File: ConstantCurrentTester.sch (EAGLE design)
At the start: 3 parts, among them U1 ATMEGA328PQFN_32, Y1 8MHz

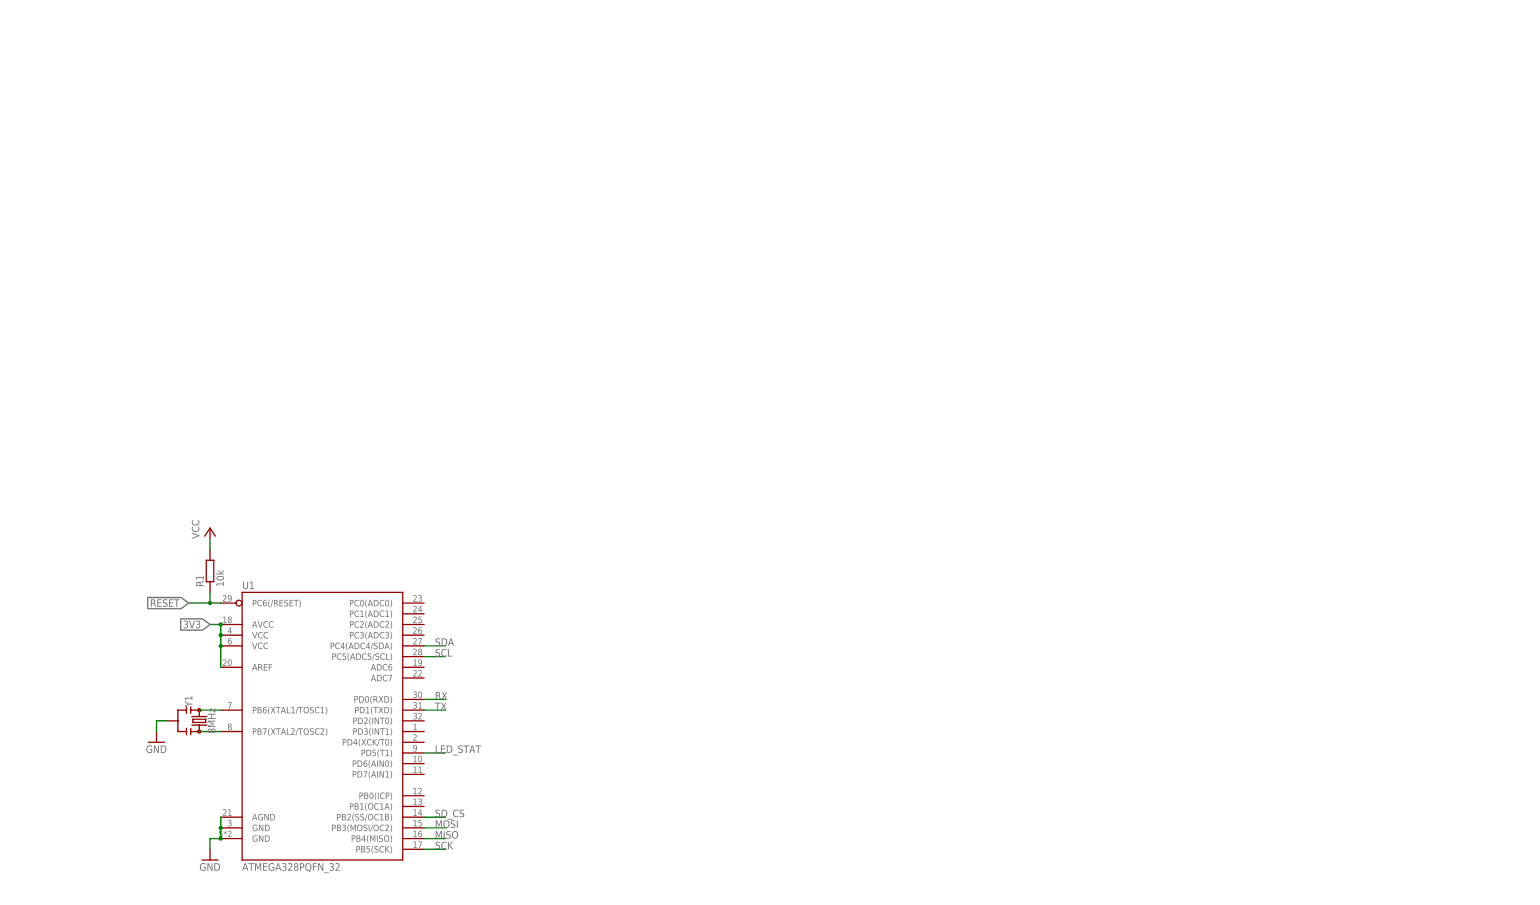
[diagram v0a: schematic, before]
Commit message: Preliminary schematic capture complete
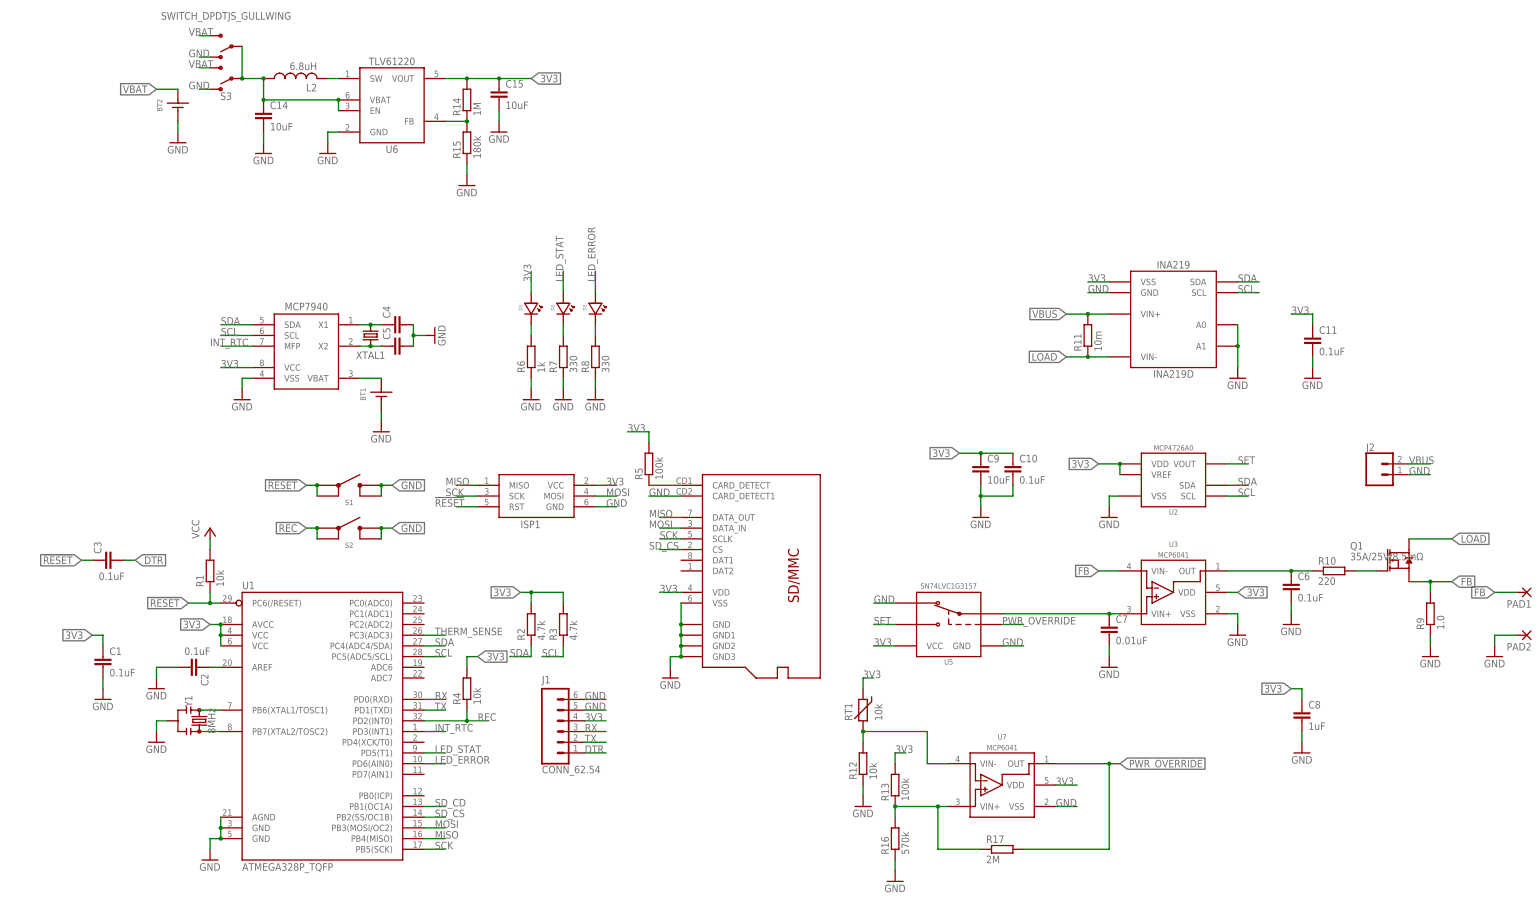
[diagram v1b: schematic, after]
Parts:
- added BT1: BATTERY_COIN12MM, bschulz:BATTERY_COIN12MM
- added BT2: BATTERY_COINAA, bschulz:BATTERY_COINAA
- added C1, C10, C11, C2, C3, C6: 0.1uF, bschulz_passives:C-EU0.1UFC0603
- added C14, C15, C9: 10uF, bschulz_passives:C-EU10UFC0805
- added C4, C5: (no value), bschulz_passives:C-EUC0603
- added C7: 0.01uF, bschulz_passives:C-EUC0603
- added C8: 1uF, bschulz_passives:C-EU1UFC0603
- added D1: LEDBLUE0603, bschulz:LEDBLUE0603
- added D2: LEDGREEN0603, bschulz:LEDGREEN0603
- added D3: LEDRED0603, bschulz:LEDRED0603
- added ISP1: AVRISP-6, bschulz:AVRISP-6
- added J1: CONN_62.54, bschulz:CONN_62.54
- added J2: (no value), bschulz:CONN_023.5MM
- added L2: 6.8uH, bschulz:INDUCTOR1008
- added PAD1, PAD2: (no value), wirepad:3,81/1,4
- added Q1: 35A/25V/8.5mΩ, bschulz:MOSFET-NCH-FDD8780
- added R10: 220, bschulz_passives:R-EU_0207/10
- added R11: 10m, bschulz_passives:R-EU_0.01R0805
- added R12: 10k, bschulz_passives:R-EU_10KR0603
- added R13, R5: 100k, bschulz_passives:R-EU_100KR0603
- added R14: 1M, bschulz_passives:R-EU_1MR0603
- added R15: 180k, bschulz_passives:R-EU_180KR0603
- added R16: 570k, bschulz_passives:R-EU_R0603
- added R17: 2M, bschulz_passives:R-EU_R0603
- added R2, R3: 4.7k, bschulz_passives:R-EU_4.7KR0603
- added R4: 10k, bschulz:R-EU_10KR0603
- added R6: 1k, bschulz_passives:R-EU_1KR0603
- added R7, R8: 330, bschulz_passives:R-EU_330R0603
- added R9: 1.0, rcl:R-EU_0617/22
- added RT1: 10k, bschulz:THERMISTOR10K
- added S1, S2: BUTTON6X6_TH, bschulz:BUTTON6X6_TH
- added S3: SWITCH_DPDTJS_GULLWING, bschulz:SWITCH_DPDTJS_GULLWING
- added U$1: MICRO_SD, bschulz:MICRO_SD
- added U$2: MCP7940SOIC, bschulz:MCP7940SOIC
- added U2: MCP4726A0SOT-23, bschulz:MCP4726A0SOT-23
- added U3, U7: MCP6041, bschulz:MCP6041
- added U4: INA219D, bschulz:INA219D
- added U5: SN74LVC1G3157SC70, bschulz:SN74LVC1G3157SC70
- added U6: TLV61220DBV, bschulz:TLV61220DBV
- added XTAL1: CRYSTAL3.2X1.5, bschulz:CRYSTAL3.2X1.5
- U1: value ATMEGA328PQFN_32 -> ATMEGA328P_TQFP; device bschulz:ATMEGA328PQFN_32 -> bschulz:ATMEGA328PTQFP_32
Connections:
- new net DRIVE: Q1.G, R10.2
- new net DTR: C3.2, J1.1
- new net FB: PAD1.P, Q1.S, R9.2, U3.VIN-
- new net FB2: R14.1, R15.2, U6.FB
- new net INT_RTC: U$2.MFP, U1.PD3(INT1)
- new net LED_ERROR: D3.ANODE, U1.PD6(AIN0)
- new net LOAD: Q1.D, R11.1, U4.VIN-
- new net N$10: C6.1, R10.1, U3.OUT
- new net N$11: R12.2, RT1.1, U7.VIN-
- new net N$12: R13.1, R16.2, R17.1, U7.VIN+
- new net N$3: C2.1, U1.AREF
- new net N$4: R5.1, U$1.CARD_DETECT
- new net N$5: C4.1, U$2.X1, XTAL1.1
- new net N$6: C5.1, U$2.X2, XTAL1.2
- new net N$7: D1.CATHODE, R6.2
- new net N$8: D2.CATHODE, R7.2
- new net N$9: D3.CATHODE, R8.2
- new net PWR_OVERRIDE: R17.2, U5.S, U7.OUT
- new net REC: R4.1, S2.1, S2.2, U1.PD2(INT0)
- new net SD_CD: U1.PB1(OC1A)
- new net SET: C7.1, U2.VOUT, U3.VIN+, U5.A, U5.B2
- new net SW1: L2.2, U6.SW
- new net THERM_SENSE: U1.PC3(ADC3)
- new net VBAT: BT1.+, BT2.+, S3.S1, S3.S2, U$2.VBAT
- new net VBUS: J2.2, R11.2, U4.VIN+
- new net VIN: C14.1, L2.1, S3.P1, S3.P2, U6.EN, U6.VBAT
- net !RESET: now also C3.1, ISP1.RST, S1.1, S1.2
- net 3V3: now also C1.1, C10.1, C11.1, C15.1, C8.1, C9.1, D1.ANODE, ISP1.VCC, J1.4, R13.2, R14.2, R2.2, R3.2, R4.2, R5.2, RT1.2, U$1.VDD, U$2.VCC, U2.VDD, U2.VREF, U3.VDD, U4.VSS, U5.VCC, U6.VOUT, U7.VDD; no longer U1.AREF
- net GND: now also BT1.-, BT2.-, C1.2, C10.2, C11.2, C14.2, C15.2, C2.2, C4.2, C5.2, C6.2, C7.2, C8.2, C9.2, ISP1.GND, J1.5, J1.6, J2.1, PAD2.P, R12.1, R15.1, R16.1, R6.1, R7.1, R8.1, R9.1, S1.3, S1.4, S2.3, S2.4, S3.O1, S3.O2, U$1.CARD_DETECT1, U$1.GND, U$1.GND1, U$1.GND2, U$1.GND3, U$1.VSS, U$2.VSS, U2.VSS, U3.VSS, U4.A0, U4.A1, U4.GND, U5.B1, U5.GND, U6.GND, U7.VSS
- net LED_STAT: now also D2.ANODE
- net MISO: now also ISP1.MISO, U$1.DATA_OUT
- net MOSI: now also ISP1.MOSI, U$1.DATA_IN
- net RX: now also J1.3
- net SCK: now also ISP1.SCK, U$1.SCLK
- net SCL: now also R3.1, U$2.SCL, U2.SCL, U4.SCL
- net SDA: now also R2.1, U$2.SDA, U2.SDA, U4.SDA
- net SD_CS: now also U$1.CS
- net TX: now also J1.2
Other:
- moved on the sheet: U1

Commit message: Adapted Schematic, layout ready for review/cleanup
Main layout complete, details and minor cleanup remain
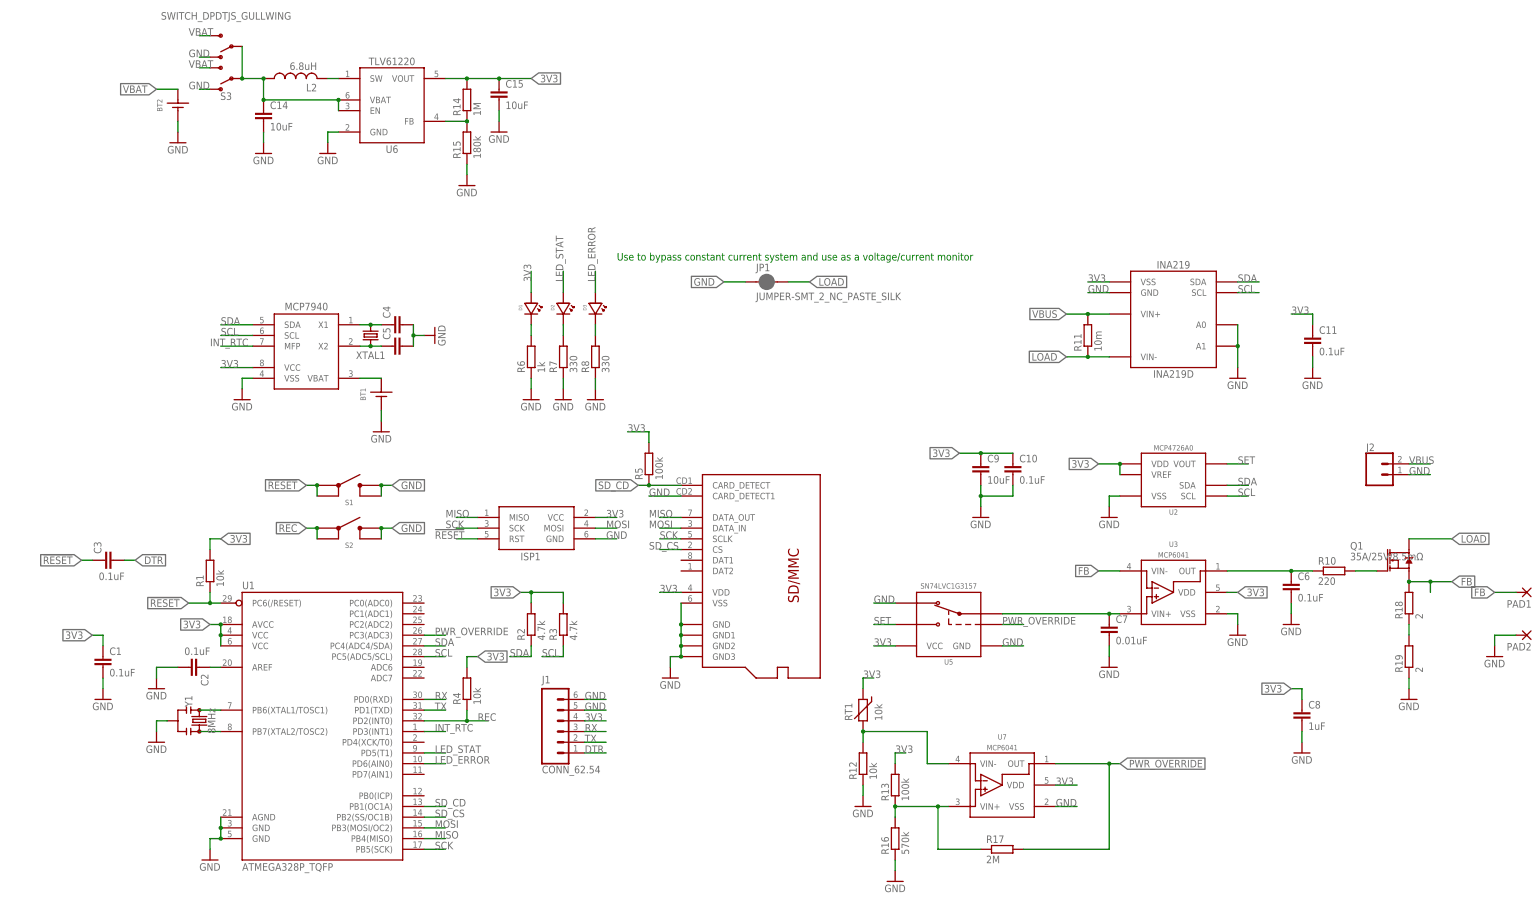
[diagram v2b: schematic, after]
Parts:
- removed R9: 1.0, rcl:R-EU_0617/22
- added JP1: JUMPER-SMT_2_NC_PASTE_SILK, SparkFun-Jumpers:JUMPER-SMT_2_NC_PASTE_SILK
- added R18, R19: 2, bschulz_passives:R-EU_R2512
- R10: device bschulz_passives:R-EU_0207/10 -> bschulz_passives:R-EU_220R0603
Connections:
- removed net N$4: R5.1, U$1.CARD_DETECT
- removed net THERM_SENSE: U1.PC3(ADC3)
- removed net VCC: R1.2
- new net N$13: R18.1, R19.2
- new net V_BACKUP: BT1.+, U$2.VBAT
- net 3V3: now also R1.2
- net FB: now also R18.2; no longer R9.2
- net GND: now also JP1.1, R19.1; no longer R9.1
- net LOAD: now also JP1.2
- net PWR_OVERRIDE: now also U1.PC3(ADC3)
- net SD_CD: now also R5.1, U$1.CARD_DETECT
- net VBAT: no longer BT1.+, U$2.VBAT
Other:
- note added: "Use to bypass constant current system and use as a voltage/current monitor"
- moved on the sheet: ISP1
